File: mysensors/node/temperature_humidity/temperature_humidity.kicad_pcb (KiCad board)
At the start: 2 copper layers, 47.5 x 21.3 mm, 31 parts, among them CON1 AVR-ISP-6, IC1 ATMEGA328P-A, P1 ANTENNA, P2 HTU21D, U1 L6920, U2 RFM69HW, X1 8MHz

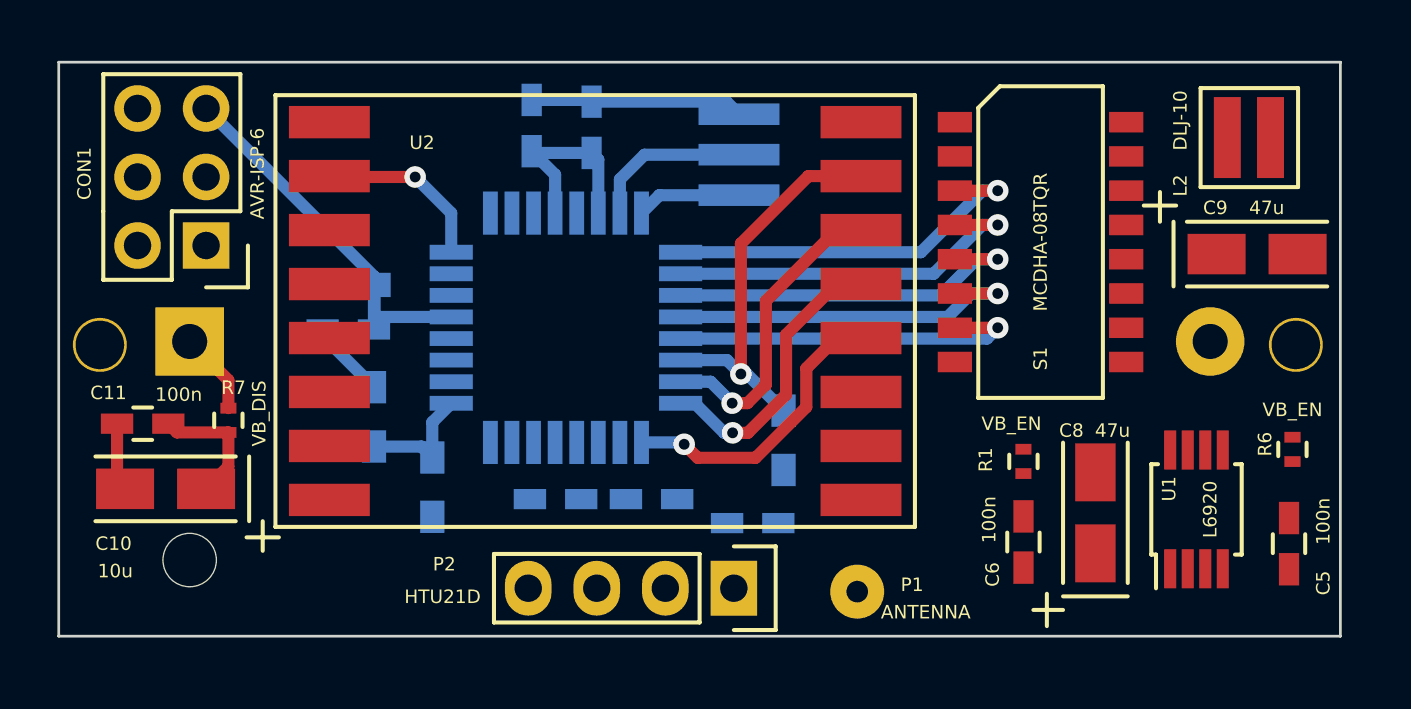
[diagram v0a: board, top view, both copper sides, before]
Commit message: [temp_hum_node] added board and all the required design files
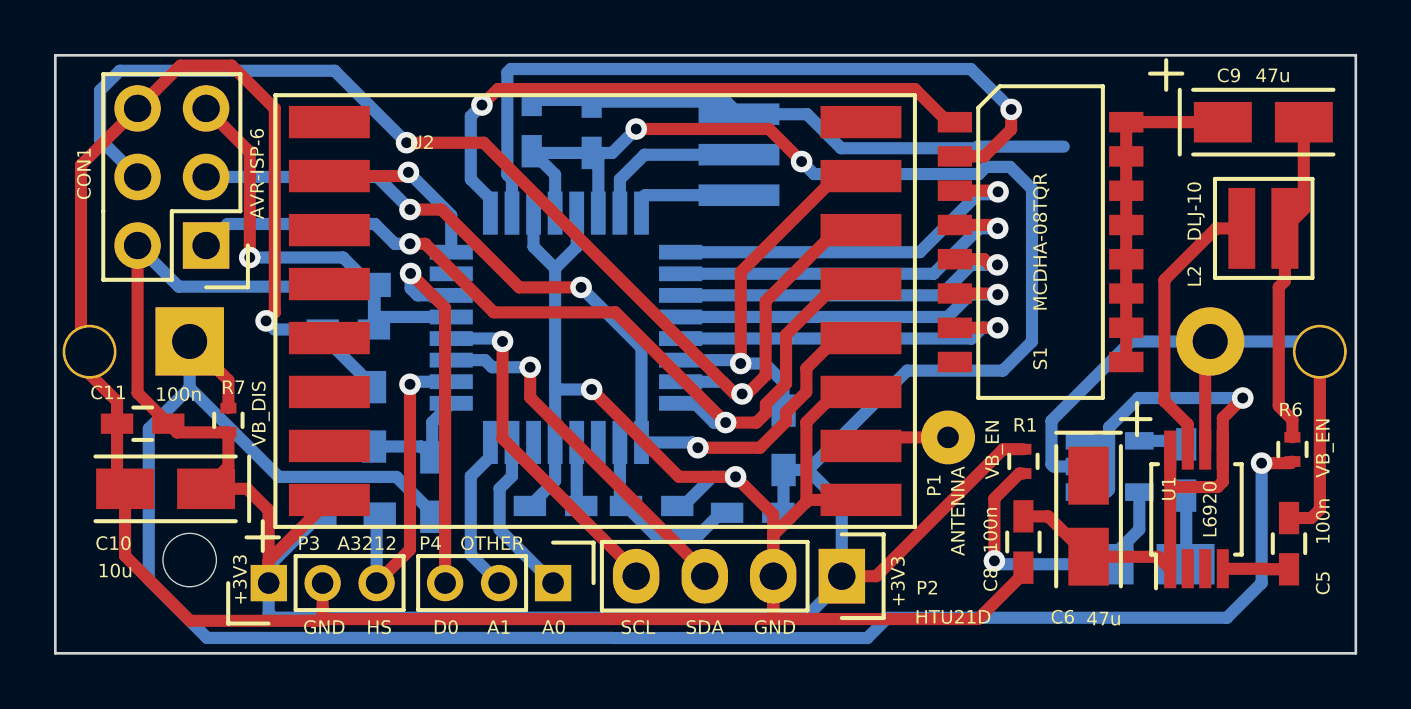
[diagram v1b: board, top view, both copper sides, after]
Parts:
- added C12: 10u, Capacitors_Tantalum_SMD:TantalC_SizeA_EIA-3216_Wave, B.Cu at (138.8, 96.1)
- added C13: 10n, Capacitors_SMD:C_0603_HandSoldering, B.Cu at (140.3, 92.6)
- added P3: A3212, Pin_Headers:Pin_Header_Straight_1x03_Pitch2.00mm, F.Cu at (106.3, 96.8)
- added P4: OTHER, Pin_Headers:Pin_Header_Straight_1x03_Pitch2.00mm, F.Cu at (116.9, 96.8)
- added R8: 51K, Resistors_SMD:R_0603_HandSoldering, B.Cu at (109.3, 94.3)
- added REF**: my_logo, myfootprints:my_logo, B.Cu at (140.7, 82.0)
- added U3: MIC5205-3.3, TO_SOT_Packages_SMD:SOT-23-5, B.Cu at (137.5, 92.5)
- L1: value BLM18HE152SN1D -> 18HE152SN1D
- moved P1 6.63 mm to (131.5, 91.4)
- moved C9 4.89 mm to (143.2, 79.8)
- moved P2 4.03 mm to (127.6, 96.6)
- moved L2 3.41 mm to (143.2, 83.7)
- moved REF** 0.92 mm to (145.3, 88.3)
- moved REF** 0.46 mm to (99.7, 88.3)
- moved L1 0.38 mm to (124.3, 94.2)
- moved C6 0.28 mm to (136.7, 94.4), turned to 270 degrees
- moved C2 0.25 mm to (120.5, 94.0)
- moved C4 0.25 mm to (117.0, 94.0)
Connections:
- IC1 pad 23: Net-(IC1-Pad23) -> /A0
- IC1 pad 24: Net-(IC1-Pad24) -> /A1
- IC1 pad 26: Net-(IC1-Pad26) -> /HALL_SENSOR
- IC1 pad 30: Net-(IC1-Pad30) -> /D0
- R1 pad 1: Net-(C6-Pad2) -> Net-(C12-Pad1)
- REF** pad : (no net) -> GND (x2)
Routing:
- net GND: track 13.4 -> 179.6 mm, vias 0 -> 3
- net +3V3: track 12.0 -> 111.7 mm, vias 0 -> 2
- net Net-(BT1-Pad1): track 3.07 -> 72.2 mm, vias 0 -> 1
- net /MOSI: track 11.5 -> 43.8 mm, vias 1 -> 2
- net /C1: track 0.00 -> 27.9 mm, vias 0 -> 1
- net Net-(C6-Pad2): track 0.00 -> 26.1 mm, vias 0 -> 1
- net /C0: track 0.00 -> 22.8 mm, vias 0 -> 1
- net /MISO: track 10.7 -> 33.0 mm, vias 1 -> 2
- net /SCK: track 11.2 -> 33.1 mm, vias 1 -> 3
- net /D0: track 0.00 -> 14.2 mm, vias 0 -> 1
- net /SDA: track 0.00 -> 13.5 mm, vias 0 -> 1
- net /SCL: track 0.00 -> 12.7 mm, vias 0 -> 1
- net /V_BOOST_IN: track 0.00 -> 12.3 mm
- net /HALL_SENSOR: track 0.00 -> 12.0 mm, vias 0 -> 1
- net Net-(C12-Pad1): track 0.00 -> 11.1 mm, vias 0 -> 1
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- added copper zone on B.Cu, net GND
- added copper zone on F.Cu, net GND
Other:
- board size 47.5 x 21.3 mm -> 48.2 x 22.2 mm
- board text added: "+3V3"
- board text added: "A0"
- board text added: "A1"
- board text added: "D0"
- board text added: "GND"
- board text added: "HS"
- board text added: "SCL"
- board text added: "SDA"

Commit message: [temp_hum] node hw design final touches
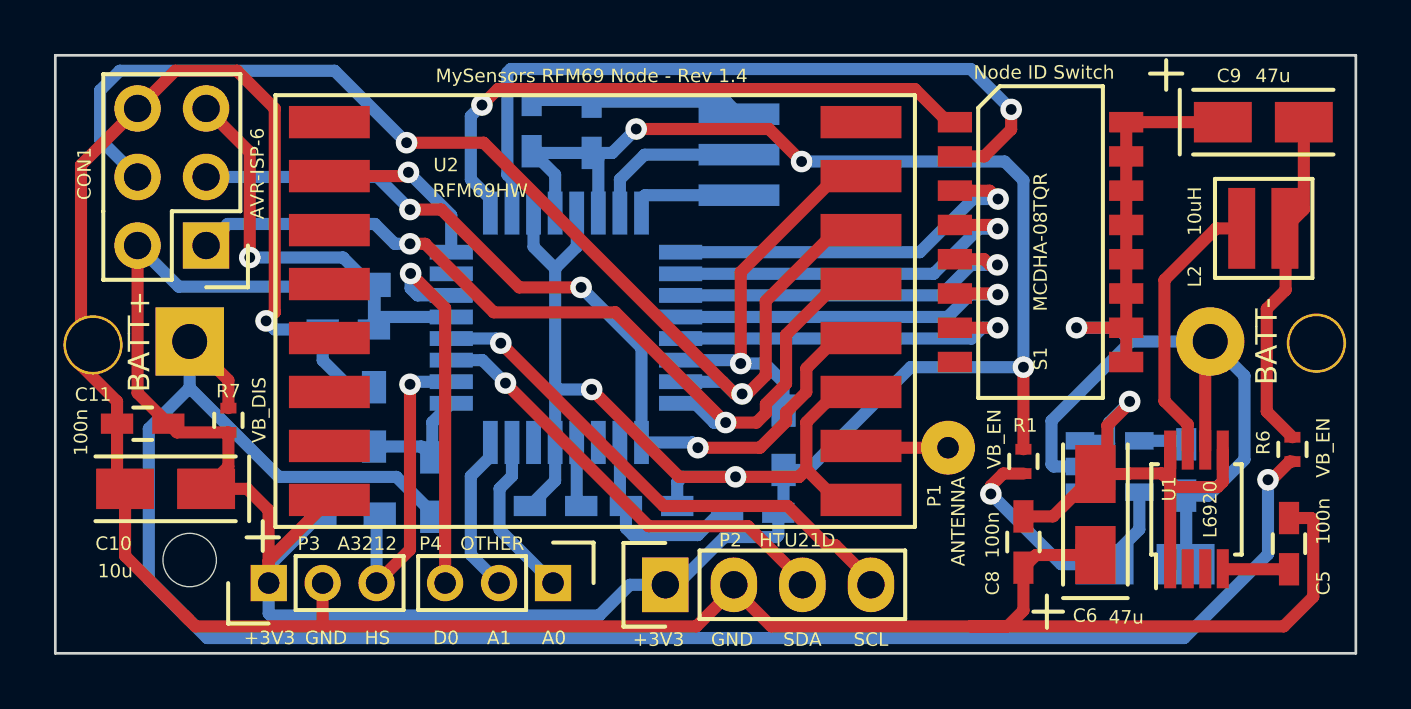
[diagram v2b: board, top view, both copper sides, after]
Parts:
- removed the REF** at (145.3, 88.3)
- removed the REF** at (99.7, 88.3)
- added REF**: MountingHole_2.2mm_M2_ISO14580_Pad, Mounting_Holes:MountingHole_2.2mm_M2_ISO14580_Pad, F.Cu at (145.2, 87.9)
- added REF**: MountingHole_2.2mm_M2_ISO14580_Pad, Mounting_Holes:MountingHole_2.2mm_M2_ISO14580_Pad, F.Cu at (99.8, 88.0)
- BT1: value 3V3 -> CR123A - 3V
- L1: value 18HE152SN1D -> BLM18HE152SN1D
- L2: value DLJ-10 -> 10uH
- moved P2 6.55 mm to (121.0, 96.9), turned to 90 degrees
- moved REF** 0.51 mm to (140.5, 81.5)
- moved P1 0.38 mm to (131.5, 91.8)
- moved C6 0.26 mm to (137.0, 94.3), turned to 90 degrees
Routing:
- net +3V3: track 111.7 -> 100.4 mm, vias 2 -> 3
- net /SCL: track 12.7 -> 19.4 mm
- net Net-(C6-Pad2): track 26.1 -> 23.0 mm
- net /SDA: track 13.5 -> 16.6 mm
- net GND: track 179.6 -> 182.7 mm, vias 3 -> 4
- net Net-(BT1-Pad1): track 72.2 -> 71.2 mm
- net Net-(C12-Pad1): track 11.1 -> 10.2 mm
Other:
- board text added: "BATT+"
- board text added: "BATT-"
- board text added: "MySensors RFM69 Node - Rev 1.4"
- board text added: "Node ID Switch"
- board text added: "Use CR123(A) 3V battery"

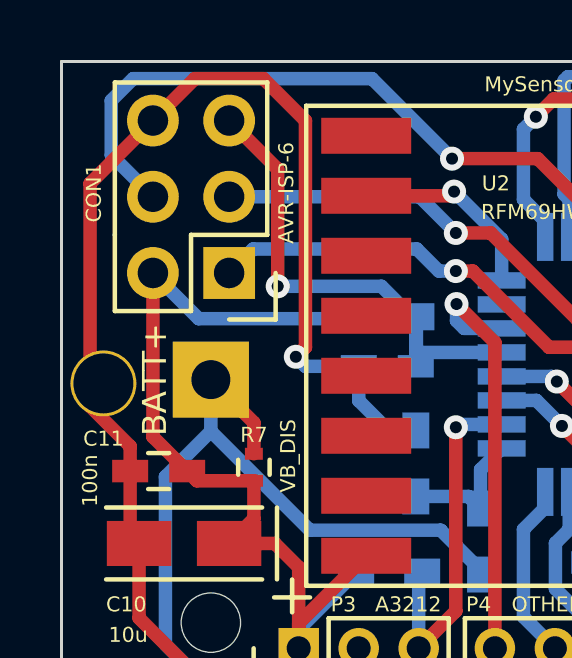
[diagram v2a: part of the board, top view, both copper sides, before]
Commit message: [temp_hum] added enlcosure freecad design
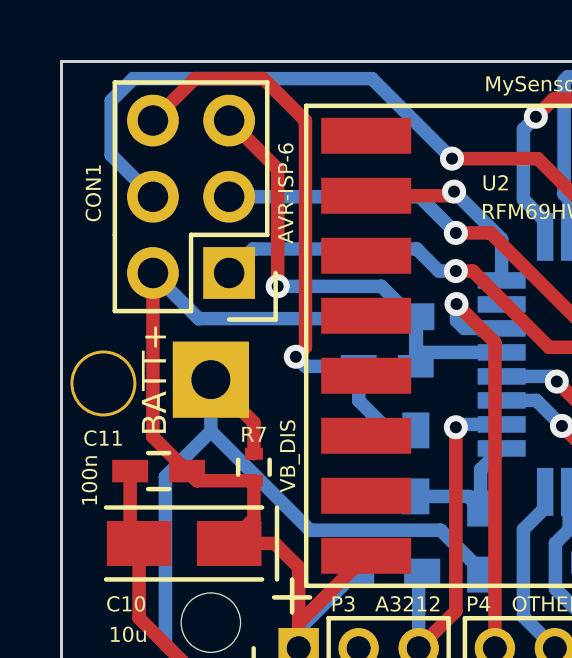
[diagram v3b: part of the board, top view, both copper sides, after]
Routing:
- net GND: track 182.7 -> 169.6 mm
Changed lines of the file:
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@@
     (links 100)
     (no_connects 0)
-    (area 91.950574 76.1733 153.032427 99.491001)
+    (area 98.374999 77.229407 146.671501 99.491001)
     (thickness 1.6)
     (drawings 19)
-    (tracks 404)
+    (tracks 400)
     (zones 0)
     (modules 38)
@@
   (segment (start 106.553 87.4395) (end 106.2355 87.122) (width 0.45) (layer B.Cu) (net 2))
   (via (at 106.2355 87.122) (size 0.8) (drill 0.4) (layers F.Cu B.Cu) (net 2))
-  (segment (start 99.3775 88.771) (end 99.3775 81.3435) (width 0.45) (layer F.Cu) (net 2) (status 10))
-  (segment (start 99.3775 81.3435) (end 101.473 79.248) (width 0.45) (layer F.Cu) (net 2) (status 20))
-  (segment (start 100.7135 90.932) (end 100.7135 90.107) (width 0.45) (layer F.Cu) (net 2) (status 10))
-  (segment (start 100.7135 90.107) (end 99.3775 88.771) (width 0.45) (layer F.Cu) (net 2) (status 20))
   (segment (start 116.948 85.176) (end 116.948 89.535) (width 0.45) (layer B.Cu) (net 2))
   (segment (start 116.948 89.535) (end 116.948 91.626) (width 0.45) (layer B.Cu) (net 2) (status 20))

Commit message: some pcb touches
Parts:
- added REF**: 1pin, myfootprints:1pin, F.Cu at (135.5, 84.3)
- added REF**: 1pin, myfootprints:1pin, F.Cu at (117.2, 87.6)
- added REF**: 1pin, myfootprints:1pin, F.Cu at (100.8, 98.4)
- added REF**: 1pin, myfootprints:1pin, F.Cu at (99.8, 98.4)
- added REF**: 1pin, myfootprints:1pin, F.Cu at (100.8, 97.4)
- added REF**: 1pin, myfootprints:1pin, F.Cu at (99.8, 97.4)
- added REF**: 1pin, myfootprints:1pin, F.Cu at (132.1, 97.8)
- added REF**: 1pin, myfootprints:1pin, F.Cu at (131.1, 97.8)
- added REF**: 1pin, myfootprints:1pin, F.Cu at (132.1, 96.8)
- added REF**: 1pin, myfootprints:1pin, F.Cu at (131.1, 96.8)
- added REF**: 1pin, myfootprints:1pin, F.Cu at (136.5, 89.2)
- added REF**: 1pin, myfootprints:1pin, F.Cu at (135.5, 83.3)
- added REF**: 1pin, myfootprints:1pin, F.Cu at (135.5, 89.2)
- added REF**: 1pin, myfootprints:1pin, F.Cu at (136.5, 88.2)
- added REF**: 1pin, myfootprints:1pin, F.Cu at (135.5, 88.2)
- added REF**: 1pin, myfootprints:1pin, F.Cu at (136.5, 87.2)
- added REF**: 1pin, myfootprints:1pin, F.Cu at (135.5, 87.2)
- added REF**: 1pin, myfootprints:1pin, F.Cu at (136.5, 86.2)
- added REF**: 1pin, myfootprints:1pin, F.Cu at (135.5, 86.2)
- added REF**: 1pin, myfootprints:1pin, F.Cu at (135.5, 82.3)
- added REF**: 1pin, myfootprints:1pin, F.Cu at (135.5, 81.3)
- added REF**: 1pin, myfootprints:1pin, F.Cu at (135.5, 80.3)
- added REF**: 1pin, myfootprints:1pin, F.Cu at (135.5, 79.3)
- added REF**: 1pin, myfootprints:1pin, F.Cu at (118.2, 88.6)
- added REF**: 1pin, myfootprints:1pin, F.Cu at (117.2, 88.6)
- added REF**: 1pin, myfootprints:1pin, F.Cu at (118.2, 87.6)
- moved REF** 1.10 mm to (141.5, 81.1)
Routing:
- net GND: track 169.6 -> 160.3 mm, vias 4 -> 3
